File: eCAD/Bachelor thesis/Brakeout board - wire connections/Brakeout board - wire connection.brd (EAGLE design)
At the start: 50 x 20 mm, 6 parts, among them IC1 VEML7700-TR

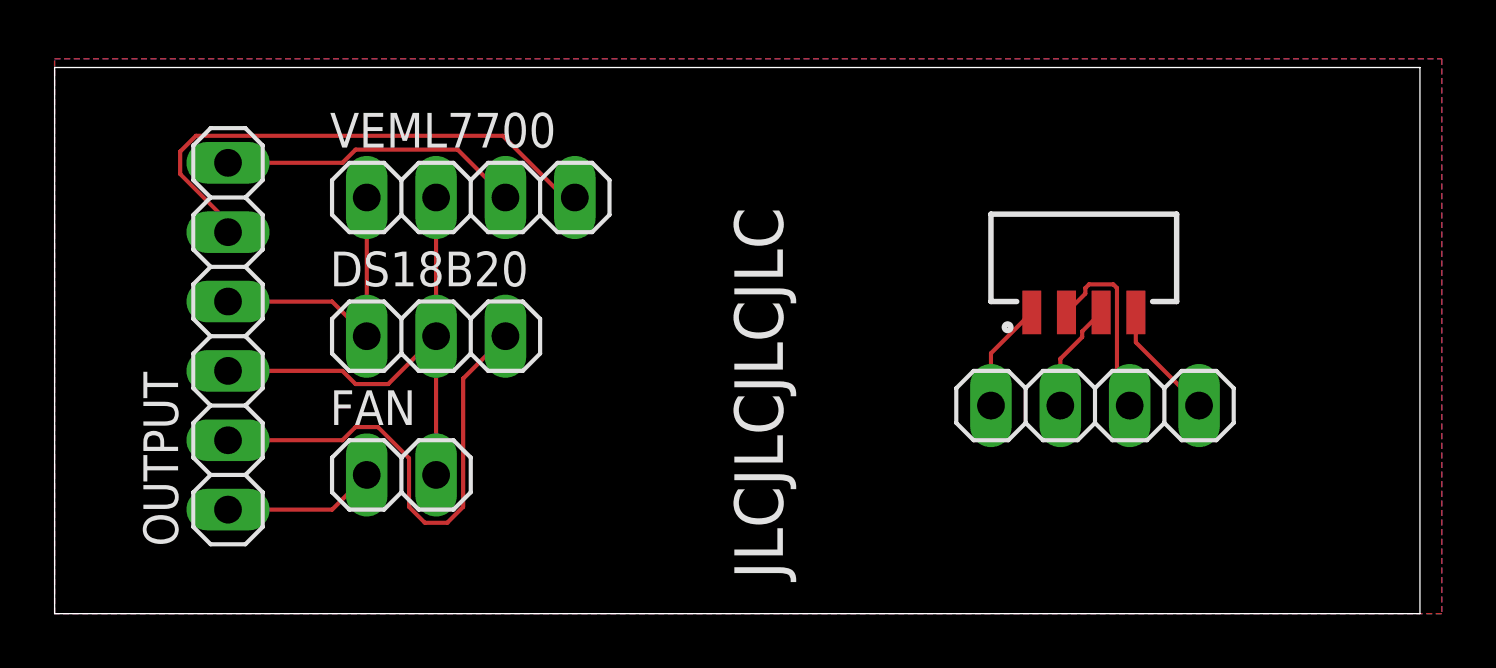
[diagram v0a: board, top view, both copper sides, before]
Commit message: Separated wire connection board and VEM7700 brakeout board, to VEML7700 board added R and C acording to datasheet
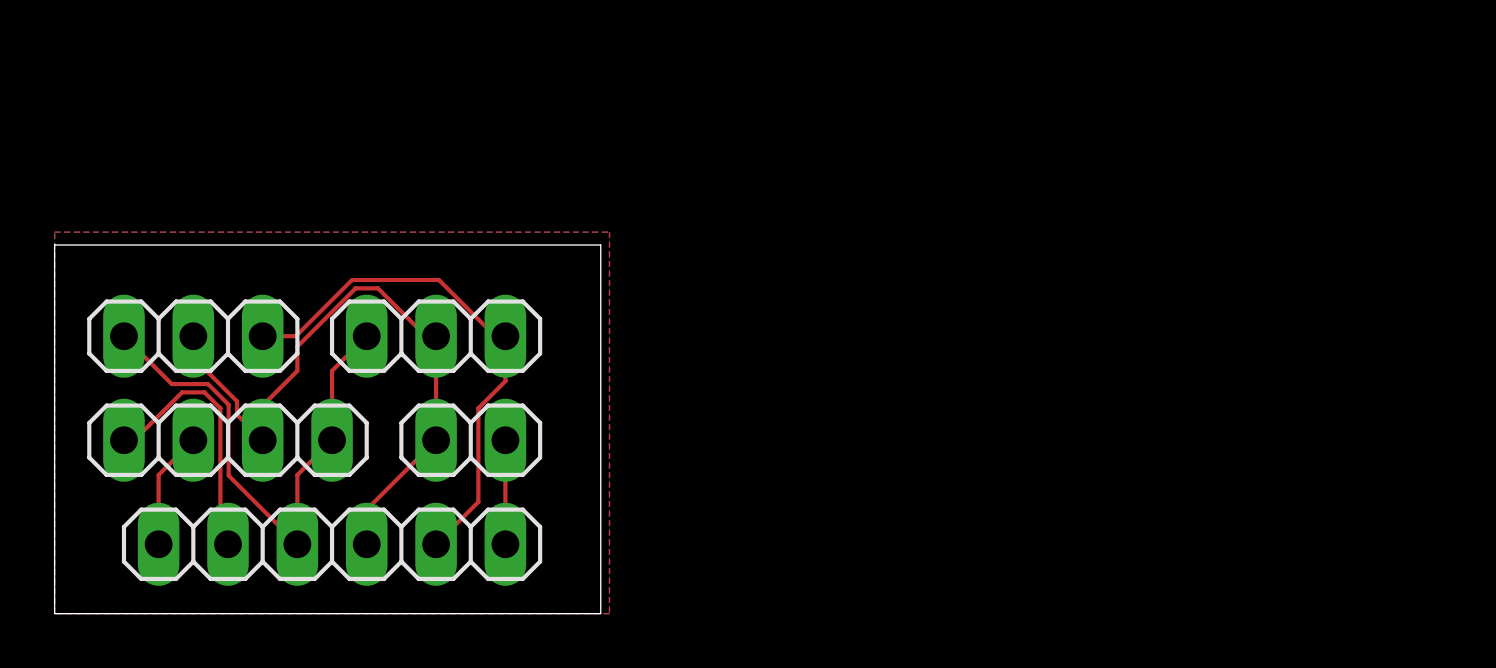
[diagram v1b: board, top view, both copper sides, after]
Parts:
- removed IC1: VEML7700-TR, 1-component-search:VEML7700
- removed VEML_BRAKEOUT: (no value), pinhead:1X04
- added DS18B20_1: (no value), pinhead:1X03
- moved VEML7700 12.6 mm to (6.35, 6.35), turned to 180 degrees
- moved OUTPUT 8.52 mm to (10.2, 2.54), turned to 180 degrees
- moved FAN 2.84 mm to (15.2, 6.35), turned to 180 degrees
- renumbered DS18B20 to DS18B20_2
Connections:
- removed net VDD: IC1.2, VEML_BRAKEOUT.3
- removed net VEML_SCL: IC1.1, IC1.4, VEML_BRAKEOUT.1, VEML_BRAKEOUT.4
- net DS18B_SIG: now also DS18B20_1.3
- net GND: now also DS18B20_1.2; no longer IC1.3, VEML_BRAKEOUT.2
- net SENSE_VDD33: now also DS18B20_1.1
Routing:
- net SCL: track 19.3 -> 9.59 mm
- net SENSE_VDD33: track 10.7 -> 19.7 mm
- net VEML_SCL: track 8.40 -> 0.00 mm
- net VDD: track 6.95 -> 0.00 mm
- net SDA: track 11.1 -> 4.34 mm
- net GND: track 22.7 -> 24.6 mm
- net VDD_FAN: track 5.61 -> 3.81 mm
- net DS18B_SIG: track 18.4 -> 19.3 mm
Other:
- board size 50 x 20 mm -> 20 x 13.5 mm
- board text removed: "JLCJLCJLCJLC"

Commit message: Final touches
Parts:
- added I2C_RES: (no value), pinhead:1X04
- moved DS18B20_1 14.2 mm to (18.3, 5.08), turned to 90 degrees
- moved OUTPUT 9.92 mm to (2.54, 8.89), turned to 90 degrees
- moved VEML7700 8.89 mm to (14.0, 10.9)
- moved FAN 5.68 mm to (10.2, 3.81), turned to 0 degrees
- moved DS18B20_2 5.12 mm to (14.6, 5.08), turned to 90 degrees
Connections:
- net GND: now also I2C_RES.2
- net SCL: now also I2C_RES.4
- net SDA: now also I2C_RES.3
- net SENSE_VDD33: now also I2C_RES.1
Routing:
- net SENSE_VDD33: track 19.7 -> 42.8 mm
- net GND: track 24.6 -> 36.0 mm
- net SDA: track 4.34 -> 14.7 mm
- net VDD_FAN: track 3.81 -> 6.88 mm
- net DS18B_SIG: track 19.3 -> 16.8 mm
- net SCL: track 9.59 -> 11.7 mm
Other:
- board size 20 x 13.5 mm -> 23.6 x 16.5 mm
